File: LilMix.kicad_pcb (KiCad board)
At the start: 2 copper layers, 79.6 x 94.4 mm, 53 parts, among them J1_L1 MONO, J1_R1 MONO, J2_L1 MONO, J2_R1 MONO, J3 STEREO, J4 MONO, J5 MONO, J6 STEREO, U1 TL074, U2 NE5532

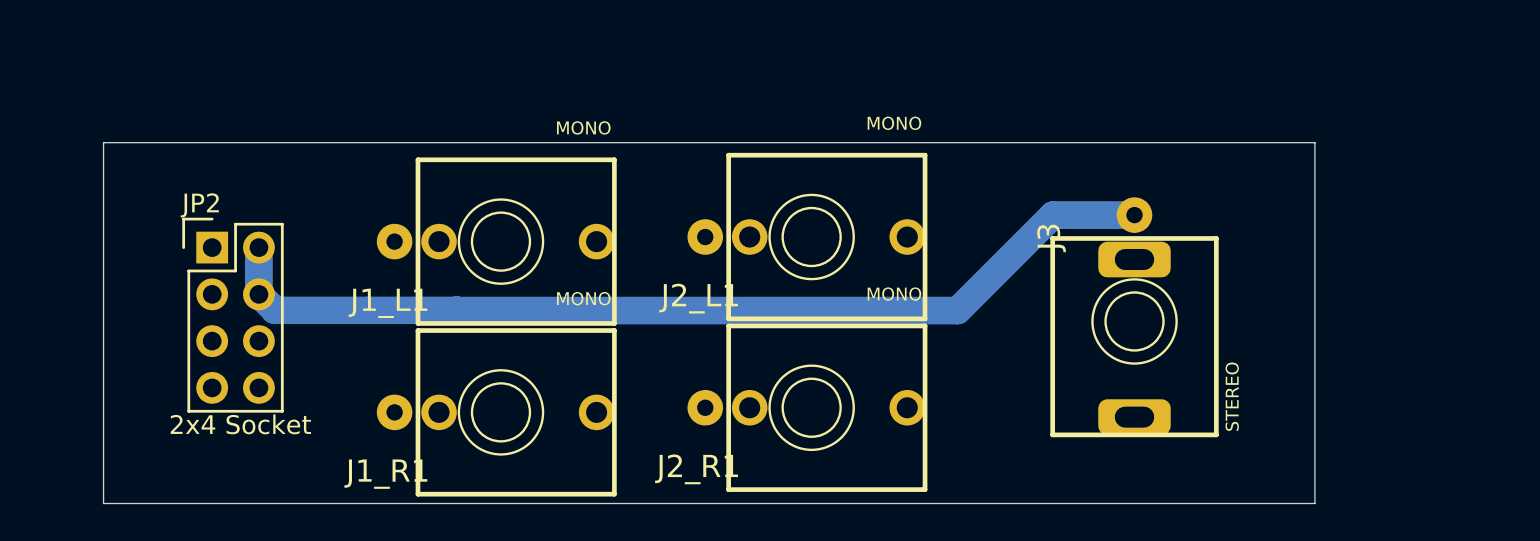
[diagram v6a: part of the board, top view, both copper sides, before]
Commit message: Added dc filtering capacitors to inputs
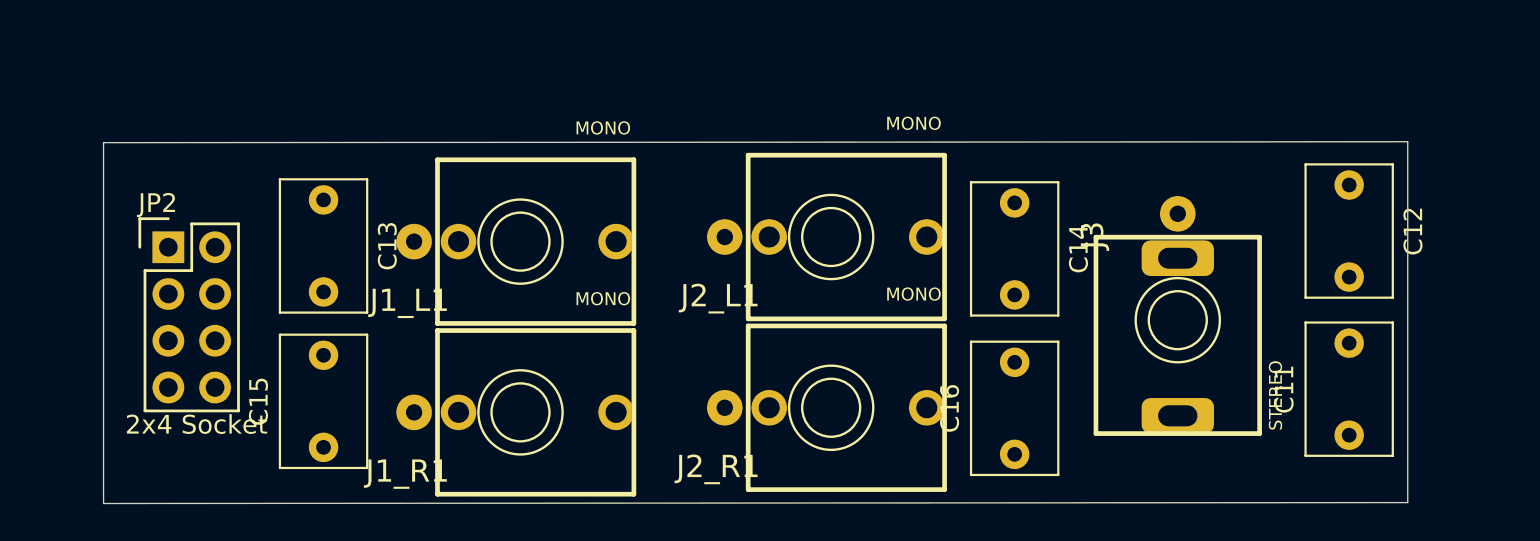
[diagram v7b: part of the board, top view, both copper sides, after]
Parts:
- added C11: 1uF, Capacitor_THT:C_Rect_L7.0mm_W4.5mm_P5.00mm, F.Cu at (160.7, 155.3)
- added C12: 1uF, Capacitor_THT:C_Rect_L7.0mm_W4.5mm_P5.00mm, F.Cu at (160.7, 141.7)
- added C13: 1uF, Capacitor_THT:C_Rect_L7.0mm_W4.5mm_P5.00mm, F.Cu at (105.0, 142.5)
- added C14: 1uF, Capacitor_THT:C_Rect_L7.0mm_W4.5mm_P5.00mm, F.Cu at (142.5, 142.7)
- added C15: 1uF, Capacitor_THT:C_Rect_L7.0mm_W4.5mm_P5.00mm, F.Cu at (105.0, 155.9)
- added C16: 1uF, Capacitor_THT:C_Rect_L7.0mm_W4.5mm_P5.00mm, F.Cu at (142.5, 156.3)
- moved JP2 2.38 mm to (96.5, 145.1)
- moved J3 2.35 mm to (151.3, 149.0)
- moved J1_L1 1.06 mm to (115.6, 144.8)
- moved J1_R1 1.06 mm to (115.6, 154.1)
- moved J2_L1 1.06 mm to (132.5, 144.5)
- moved J2_R1 1.06 mm to (132.5, 153.8)
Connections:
- J1_R1 pad 3: J1_R_B -> Net-(C15-Pad2)
- J2_R1 pad 3: J2_R_B -> Net-(C16-Pad2)
- J3 pad 1: J3_L_B -> Net-(C11-Pad2)
- J3 pad 3: J3_R_B -> Net-(C12-Pad1)
- JP2 pad 5: J1_INSERT -> J1_L_B
- JP2 pad 7: J2_INSERT -> J2_L_B
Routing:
- net GND_B: track 52.6 -> 0.00 mm
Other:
- outline, holes or cut-outs redrawn

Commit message: Nearly complete routings
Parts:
- JP2: moved to B.Cu
- moved JP2 2.71 mm to (99.2, 145.0), turned to 180 degrees
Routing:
- net GND: track 181.0 -> 304.1 mm, vias 1 -> 4
- net J3_L_B: track 0.00 -> 87.6 mm
- net GND_B: track 0.00 -> 83.2 mm
- net +12V: track 21.2 -> 96.7 mm, vias 0 -> 2
- net J2_L_B: track 0.00 -> 70.0 mm
- net J3_R_B: track 0.00 -> 65.0 mm
- net Net-(R13-Pad2): track 4.46 -> 64.6 mm, vias 0 -> 2
- net J2_R_B: track 0.00 -> 48.4 mm
- net Net-(C6-Pad2): track 29.4 -> 64.7 mm, vias 1 -> 2
- net R_INV: track 26.9 -> 59.8 mm, vias 2 -> 3
- net J2_INSERT: track 0.00 -> 24.9 mm
- net Net-(C10-Pad1): track 40.5 -> 60.3 mm, vias 1 -> 3
- net Net-(C10-Pad2): track 35.5 -> 55.1 mm, vias 1 -> 2
- net Net-(R11-Pad2): track 14.8 -> 33.1 mm
- net J1_INSERT: track 0.00 -> 17.0 mm
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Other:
- outline, holes or cut-outs redrawn
